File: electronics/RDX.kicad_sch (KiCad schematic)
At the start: 10 parts, among them J1 Raspberry_Pi_2_3, U1 PCA9685PW

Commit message: electronics progress
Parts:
- removed J2, J3: ~, symbol Connector_Generic:Conn_01-02
- added IO2, J_IO1, MISC: DE9_Socket, symbol Connector:DE9_Socket
- added J11: Conn_01x06, symbol Connector_Generic:Conn_01x06
- added J_SP1, J_SP2, J_SP3, J_SP4: Conn_01x04, symbol Connector_Generic:Conn_01x04
- added J_SV1, J_SV2, J_SV3, J_SV4, J_SV5, J_SV6: Conn_01x03, symbol Connector_Generic:Conn_01x03
- added PSU.J2, PSU.J3: ~, symbol RDX_Comp:Conn_01-02
- added SW1: RotaryEncoder_Switch, symbol Device:RotaryEncoder_Switch
- added U2: EA_T123X-I2C, Display:EA_T123X-I2C, symbol Display_Character:EA_T123X-I2C
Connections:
- net +36V: now also PSU.J2.1 (A)
- net +5V: now also U1.28 (VDD)
- net 5V_PWR: now also J_SV1.2 (Pin_2), J_SV2.2 (Pin_2), J_SV3.2 (Pin_2), J_SV4.2 (Pin_2), J_SV5.2 (Pin_2), J_SV6.2 (Pin_2)
- net GND: now also U1.14 (VSS), J_SV1.3 (Pin_3), J_SV2.3 (Pin_3), J_SV3.3 (Pin_3), J_SV4.3 (Pin_3), J_SV5.3 (Pin_3), J_SV6.3 (Pin_3), PSU.J3.1 (A)
- net at U1.10 (LED4): now also J_SV5.1 (Pin_1)
- net at U1.11 (LED5): now also J_SV6.1 (Pin_1)
- net at U1.6 (LED0): now also J_SV1.1 (Pin_1)
- net at U1.7 (LED1): now also J_SV2.1 (Pin_1)
- net at U1.8 (LED2): now also J_SV3.1 (Pin_1)
- net at U1.9 (LED3): now also J_SV4.1 (Pin_1)
- net IO1_2: now reaches J1.11 (GPIO17)
- net IO1_3: now reaches J1.13 (GPIO27)
- net IO1_1: now reaches J1.7 (GCLK0/GPIO4)
- net at PSU.PS13.1 (-VIN): now also PSU.J3.3 (B)
- net at PSU.PS12.1 (-VIN): now also PSU.J3.2 (B)
- net at PSU.PS13.3 (+VIN): now also PSU.J2.3 (B)
- net at PSU.PS12.3 (+VIN): now also PSU.J2.2 (B)
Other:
- moved on the sheet: J1, U1

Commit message: improving electronics
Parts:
- removed J1: Raspberry_Pi_2_3, symbol Connector:Raspberry_Pi_2_3
- removed J_SP2, J_SP3, J_SP4: Conn_01x04, symbol Connector_Generic:Conn_01x04
- added J1, PSU.J4: ~, symbol RDX_Comp:Conn_01-02
- added PSU.J5: ~, symbol RDX_Comp:Conn_01-04
- added STEP.U1: Generic PWM Stepper Controller, symbol RDX_Comp:PWMStepperCtrl
- added U3: RPi_Generic, symbol RDX_Comp:RPi_Board
- renumbered J_SP1 to J_STEP.J1
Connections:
- net +36V: now also PSU.J2.; no longer PSU.J2.1 (A)
- net +5V: now also U2.2 (VDD), PSU.J5., U3.2 (+5V); no longer PSU.PS13.8 (+VOUT)
- net 5V_PWR: now also PSU.J4.; no longer PSU.PS12.8 (+VOUT)
- net GND: now also PSU.J3., U1.1 (A0), U1.2 (A1), U1.24 (A5), U1.3 (A2), U1.4 (A3), U1.5 (A4); no longer PSU.J3.1 (A)
- net IO1_1: now also U3.7 (IO4)
- net IO1_2: now also U3.11 (IO17)
- net IO1_3: now also U3.13 (IO27)
- net at PSU.PS12.1 (-VIN): now also PSU.J3.; no longer PSU.J3.2 (B)
- net at PSU.PS13.1 (-VIN): now also PSU.J3.; no longer PSU.J3.3 (B)
- net at PSU.PS12.3 (+VIN): now also PSU.J2.; no longer PSU.J2.2 (B)
- net at PSU.PS13.3 (+VIN): now also PSU.J2.; no longer PSU.J2.3 (B)
- net at J_STEP.J1.1 (Pin_1): now also STEP.U1. (B2)
- net at J_STEP.J1.2 (Pin_2): now also STEP.U1. (B2)
- net at J_STEP.J1.3 (Pin_3): now also STEP.U1. (B2)
- net at J_STEP.J1.4 (Pin_4): now also STEP.U1. (B2)
- new net: PSU.J4., PSU.PS12.8 (+VOUT)
- new net: J1., U3.17 (+3.3V)
- new net: PSU.J5., PSU.PS13.8 (+VOUT)
- new net IO1_4: U3.15 (IO22)
- new net IO1_GND: U3.9 (GND)
- new net IO1_VCC: J1.
- new net IO2_1: U3.19 (IO10)
- new net IO2_2: U3.21 (IO9)
- new net IO2_3: U3.23 (IO11)
- new net IO2_GND: U3.25 (GND)
- new net IO2_VCC: J1.
- new net MISC_3.3V: U3.1 (+3.3V)
- new net MISC_5V: U3.4 (+5V)
- new net SC1_STEP: U3.31 (IO6)
- new net SC2_STEP: U3.33 (IO13)
- new net SC3_STEP: U3.35 (IO19)
- new net SC4_STEP: U3.37 (IO26)
- new net SC_EN: U3.29 (IO5)
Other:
- note added: "Main PSU (PSU.PS1) supports up to 3 connections"
- moved on the sheet: IO2, J11, J_IO1, J_STEP.J1, J_SV1, J_SV2, J_SV3, J_SV4, J_SV5, J_SV6, MISC, U1

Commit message: finished first draft of electronics
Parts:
- removed SW1: RotaryEncoder_Switch, symbol Device:RotaryEncoder_Switch
- removed U2: EA_T123X-I2C, Display:EA_T123X-I2C, symbol Display_Character:EA_T123X-I2C
- added CTRL.J2, CTRL.J3, STEP.J1, STEP.J2, STEP.J3, STEP.J4: ~, symbol RDX_Comp:Conn_01-03
- added OUT.STEP2, OUT.STEP3, OUT.STEP4: Conn_01x04, symbol Connector_Generic:Conn_01x04
- added PER.M1: Fan_4pin, symbol Motor:Fan_4pin
- added PER.U1: 1602A_I2C, symbol RDX_Comp:LCD1602A_I2C
- added PSU.J11, PSU.J12: ~, symbol RDX_Comp:Conn_01-05
- added PSU.J21, PSU.J22, PSU.J32: ~, symbol RDX_Comp:Conn_01-02
- added PSU.SW2: SW_SPST, symbol Switch:SW_SPST
- added STEP.J5: ~, symbol RDX_Comp:Conn_01-04
- added STEP.U2, STEP.U3, STEP.U4: Generic PWM Stepper Controller, symbol RDX_Comp:PWMStepperCtrl
- added SW1: Rotary Encoder Module, symbol RDX_Comp:RotEncoderMod
- renumbered J1 to CTRL.J1, U3 to CTRL.U1, J_IO1 to OUT.IO1, IO2 to OUT.IO2, MISC to OUT.MISC, J11 to OUT.POW, J_STEP.J1 to OUT.STEP1, J_SV1 to OUT.SV1, J_SV2 to OUT.SV2, J_SV3 to OUT.SV3, J_SV4 to OUT.SV4, J_SV5 to OUT.SV5, J_SV6 to OUT.SV6, PSU.J2 to PSU.J01, PSU.J3 to PSU.J02, PSU.J4 to PSU.J31, PSU.J5 to PSU.J41
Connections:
- net +12V: now also OUT.POW.2 (Pin_2), PER.M1.2 (+), PSU.J21.; no longer PSU.PS11.8 (+VOUT)
- net +36V: now also OUT.POW.1 (Pin_1), STEP.U1. (B2), PSU.J11., STEP.U2. (B2), STEP.U3. (B2), STEP.U4. (B2); no longer PSU.J01., PSU.PS1.3 (DC+), PSU.PS11.3 (+VIN)
- net +5V: now also PER.U1. (GND), SW1. (GND)
- net 5V_PWR: now also OUT.POW.3 (Pin_3)
- net GND: now also CTRL.U1.14 (GND), CTRL.U1.30 (GND), CTRL.U1.34 (GND), CTRL.U1.6 (GND), OUT.POW.4 (Pin_4), OUT.POW.5 (Pin_5), OUT.POW.6 (Pin_6), STEP.U1. (B2), PER.M1.1 (-), PER.U1. (GND), PSU.J12., PSU.J22., PSU.J32., STEP.J1., STEP.J2., STEP.J3., STEP.J4., STEP.J5., STEP.U2. (B2), STEP.U3. (B2), STEP.U4. (B2), SW1. (GND); no longer PSU.J02., PSU.PS1.4 (DC-), PSU.PS11.1 (-VIN), PSU.PS11.7 (-VOUT), PSU.PS12.7 (-VOUT)
- net IO1_1: now also OUT.IO1.2
- net IO1_2: now also OUT.IO1.3
- net IO1_3: now also OUT.IO1.7
- net IO1_4: now also OUT.IO1.8
- net IO1_GND: now also OUT.IO1.4, OUT.IO1.9
- net IO1_VCC: now also OUT.IO1.1, OUT.IO1.6
- net IO2_1: now also OUT.IO2.2
- net IO2_2: now also OUT.IO2.3
- net IO2_3: now also OUT.IO2.7
- net IO2_GND: now also OUT.IO2.4, OUT.IO2.9
- net IO2_VCC: now also OUT.IO2.1, OUT.IO2.6
- net MISC_3.3V: now also OUT.MISC.6
- net MISC_5V: now also OUT.MISC.1
- net SC1_STEP: now also STEP.U1. (B2)
- net SC2_STEP: now also STEP.U2. (B2)
- net SC3_STEP: now also STEP.U3. (B2)
- net SC4_STEP: now also STEP.U4. (B2)
- net SC_EN: now also STEP.U1. (B2), STEP.U2. (B2), STEP.U3. (B2), STEP.U4. (B2)
- net IO2_4: now reaches OUT.IO2.8
- net IO2_4: now also CTRL.U1.24 (IO8)
- net MISC_SDA: now reaches OUT.MISC.2
- net MISC_SCL: now reaches OUT.MISC.3
- net MISC_CS1: now reaches OUT.MISC.4
- net MISC_CS1: now also CTRL.U1.26 (IO7)
- net MISC_GND: now reaches OUT.MISC.5
- net MISC_GND: now also CTRL.U1.20 (GND), OUT.MISC.9
- net MISC_TX: now reaches OUT.MISC.7
- net MISC_TX: now also CTRL.U1.8 (IO14)
- net MISC_RX: now reaches OUT.MISC.8
- net MISC_RX: now also CTRL.U1.12 (IO18)
- net ROT_DT: now reaches CTRL.U1.16 (IO23)
- net ROT_DT: now also SW1. (GND)
- net ROT_CL: now reaches CTRL.U1.18 (IO24)
- net ROT_CL: now also SW1. (GND)
- net ROT_SW: now reaches CTRL.U1.22 (IO25)
- net ROT_SW: now also SW1. (GND)
- net at CTRL.U1.3 (IO2): now also CTRL.J2.
- net SC1_DIR: now reaches CTRL.U1.32 (IO12)
- net SC2_DIR: now reaches CTRL.U1.36 (IO16)
- net SC2_DIR: now also STEP.U2. (B2)
- net SC3_DIR: now reaches CTRL.U1.38 (IO20)
- net SC3_DIR: now also STEP.U3. (B2)
- net at CTRL.U1.39 (GND): now also STEP.J5.
- net SC4_DIR: now reaches CTRL.U1.40 (IO21)
- net SC4_DIR: now also STEP.U4. (B2)
- net at CTRL.U1.5 (IO3): now also CTRL.J3.
- new net: PSU.J01., PSU.PS1.3 (DC+), PSU.PS11.3 (+VIN), PSU.SW2.1 (A)
- new net: PSU.J11., PSU.SW2.2 (B)
- new net: PSU.J02., PSU.J12., PSU.PS1.4 (DC-), PSU.PS11.1 (-VIN)
- new net: STEP.J2., STEP.U2. (B2) (x3)
- new net: OUT.STEP4.1 (Pin_1), STEP.U4. (B2)
- new net: OUT.STEP4.2 (Pin_2), STEP.U4. (B2)
- new net: OUT.STEP4.3 (Pin_3), STEP.U4. (B2)
- new net: OUT.STEP4.4 (Pin_4), STEP.U4. (B2)
- new net: STEP.J4., STEP.U4. (B2) (x3)
- new net: STEP.J1., STEP.U1. (B2) (x3)
- new net: PSU.J22., PSU.PS11.7 (-VOUT)
- new net: OUT.STEP3.1 (Pin_1), STEP.U3. (B2)
- new net: OUT.STEP3.2 (Pin_2), STEP.U3. (B2)
- new net: OUT.STEP3.3 (Pin_3), STEP.U3. (B2)
- new net: OUT.STEP3.4 (Pin_4), STEP.U3. (B2)
- new net: PSU.J32., PSU.PS12.7 (-VOUT)
- new net: STEP.J3., STEP.U3. (B2) (x3)
- new net: OUT.STEP2.1 (Pin_1), STEP.U2. (B2)
- new net: OUT.STEP2.2 (Pin_2), STEP.U2. (B2)
- new net: OUT.STEP2.3 (Pin_3), STEP.U2. (B2)
- new net: OUT.STEP2.4 (Pin_4), STEP.U2. (B2)
- new net: PSU.J21., PSU.PS11.8 (+VOUT)
- new net FAN_PWM: CTRL.U1.12 (IO18), PER.M1.4 (PWM)
- no-connect marks 2 -> 17
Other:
- note added: "Access to the controllers different power levels"
- note added: "IO Plugs provide fast access to the RPis GPIO pins with addtional voltage and ground pins (Optimized for endstop-switches)"
- note added: "LCD-Display"
- note added: "PSU.J12 (36V)"
- note added: "PSU.J22 (12V)"
- note added: "PSU.J32 (5V PWR)"
- note added: "PSU.J32 (5V)"
- note added: "Power connection from PSU"
- note added: "Rot-Encoder"
- note added: "STEP.J1 - STEP.J4 (5V)"
- note added: "STEP.J5 (5V)"
- note added: "Servo-Driver"
- note added: "The MISC plug maps miscellaneous pins, busses and interfaces like I2C. UART and additions to OUT.IO2 SPI"
- note added: "The controller includes 3 high performace stepper drivers that can be calibrated for microstepping manually See the table for pin mappings to the RPi GPIOs"
- moved on the sheet: CTRL.J1, CTRL.U1, OUT.IO1, OUT.IO2, OUT.MISC, OUT.POW, OUT.STEP1, OUT.SV1, OUT.SV2, OUT.SV3, OUT.SV4, OUT.SV5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

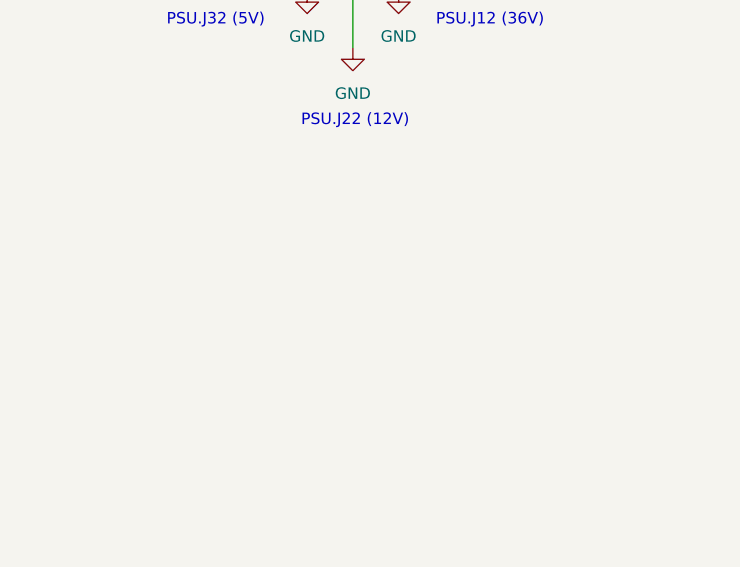
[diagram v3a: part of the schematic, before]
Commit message: improved electronics documentation and created PDF
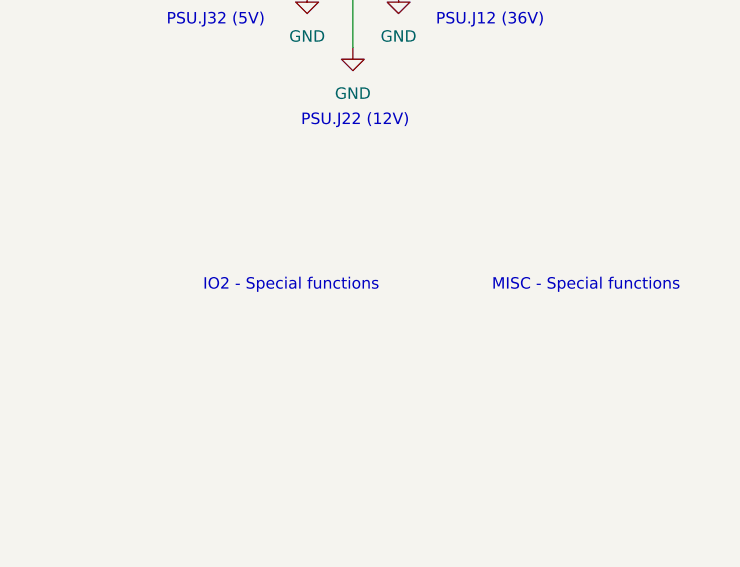
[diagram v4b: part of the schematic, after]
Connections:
- new net: STEP.J2., STEP.U2. (B2) (x3)
- new net: STEP.J4., STEP.U4. (B2) (x3)
- new net: STEP.J1., STEP.U1. (B2) (x3)
- new net: STEP.J3., STEP.U3. (B2) (x3)
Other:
- note added: "IO2 - Special functions"
- note added: "MISC - Special functions"
